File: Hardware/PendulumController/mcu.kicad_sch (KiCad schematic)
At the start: 21 parts, among them J201 Tag Connect, SW201 RESET, SW202 START_SW, SW203 STOP/MODE_SW, U201 ATmega328P-A, Y201 16mHz

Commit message: Cleanup board layout, cleanup firmware and go to bed, this is a sturdy place to start a new project!
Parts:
- J201: value Tag Connect -> ICSP
- U201: value ATmega328P-A -> ATmega328P
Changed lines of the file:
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@@
     (in_bom yes) (on_board yes)
     (property "Reference" "J201" (id 0) (at 41.91 147.32 0))
-    (property "Value" "Tag Connect" (id 1) (at 41.275 162.56 0))
+    (property "Value" "ICSP" (id 1) (at 41.91 162.56 0))
     (property "Footprint" "Connector:Tag-Connect_TC2050-IDC-FP_2x05_P1.27mm_Vertical" (id 2) (at 40.64 154.94 0)
       (effects (font (size 1.27 1.27)) hide)
@@
       (effects (font (size 1.27 1.27)) (justify left))
     )
-    (property "Value" "ATmega328P-A" (id 1) (at 43.815 116.84 0)
+    (property "Value" "ATmega328P" (id 1) (at 43.815 116.84 0)
       (effects (font (size 1.27 1.27)) (justify left))
     )

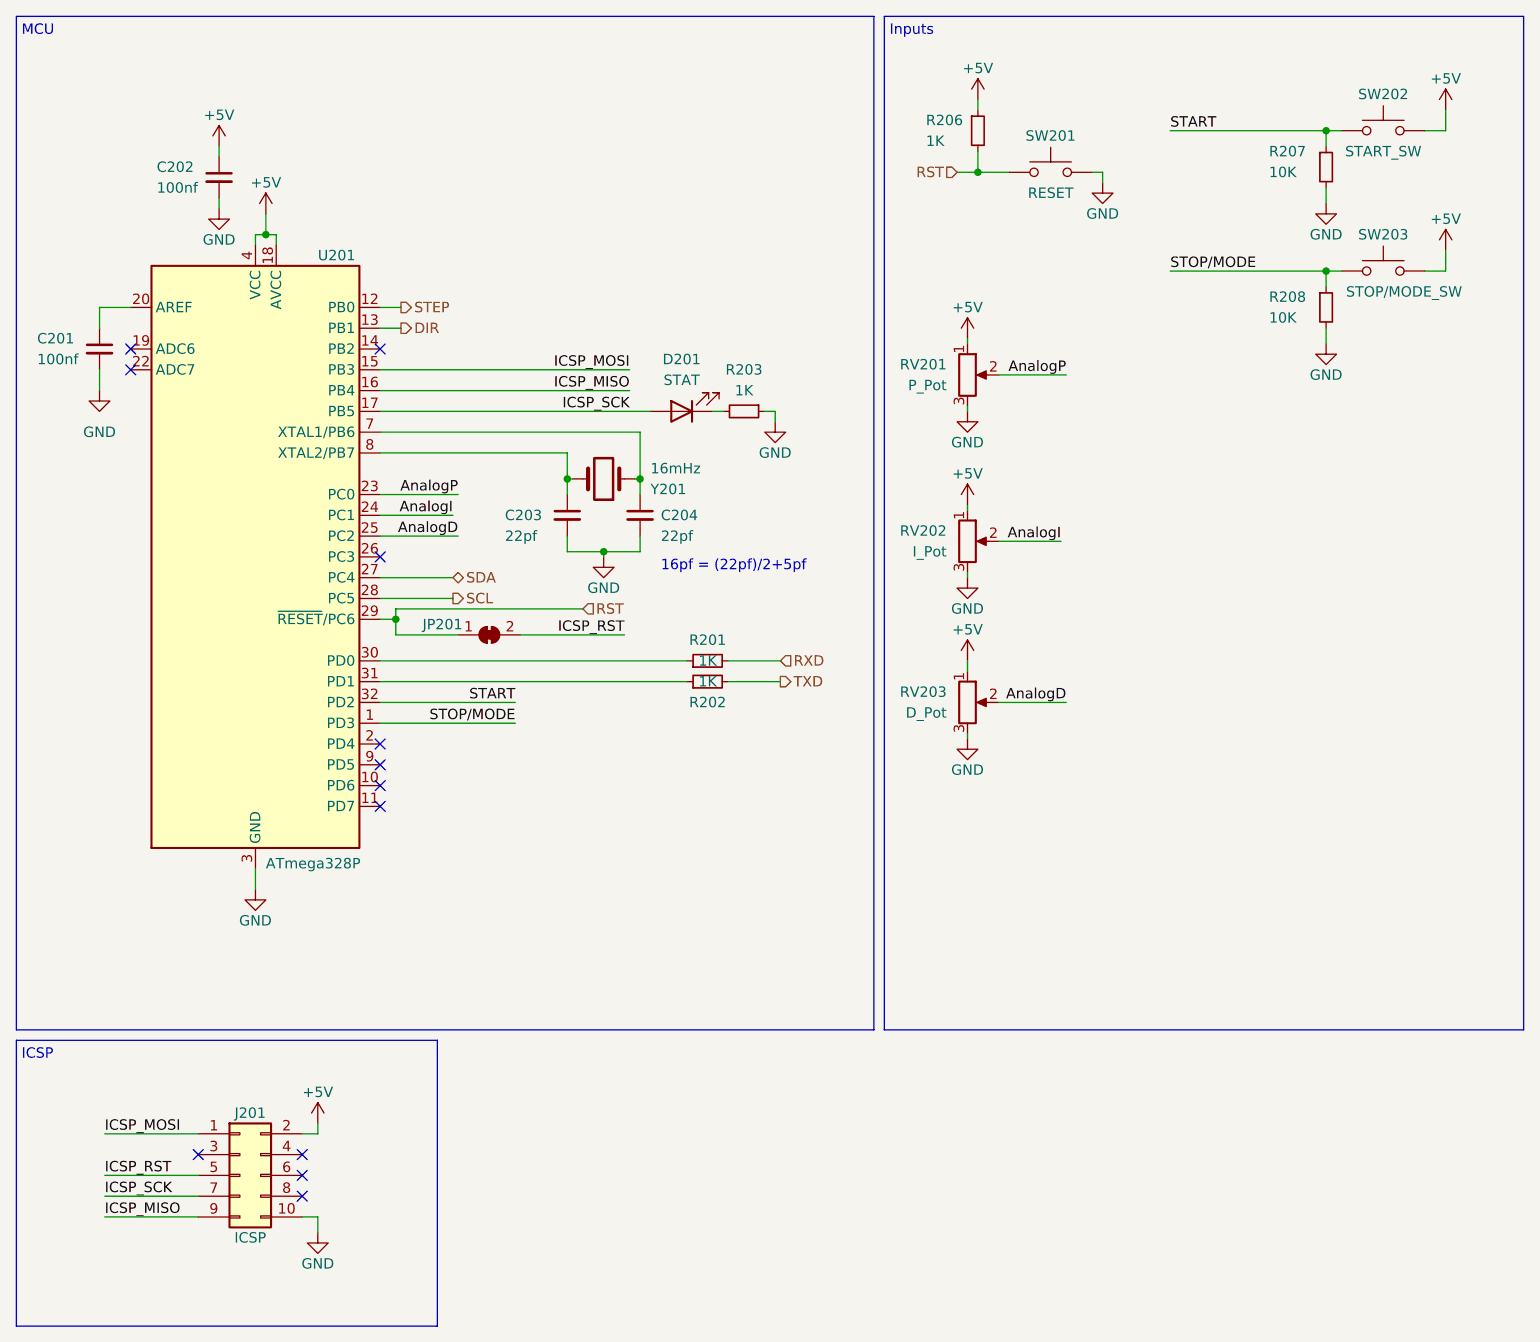
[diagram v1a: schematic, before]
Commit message: Add TFT connector
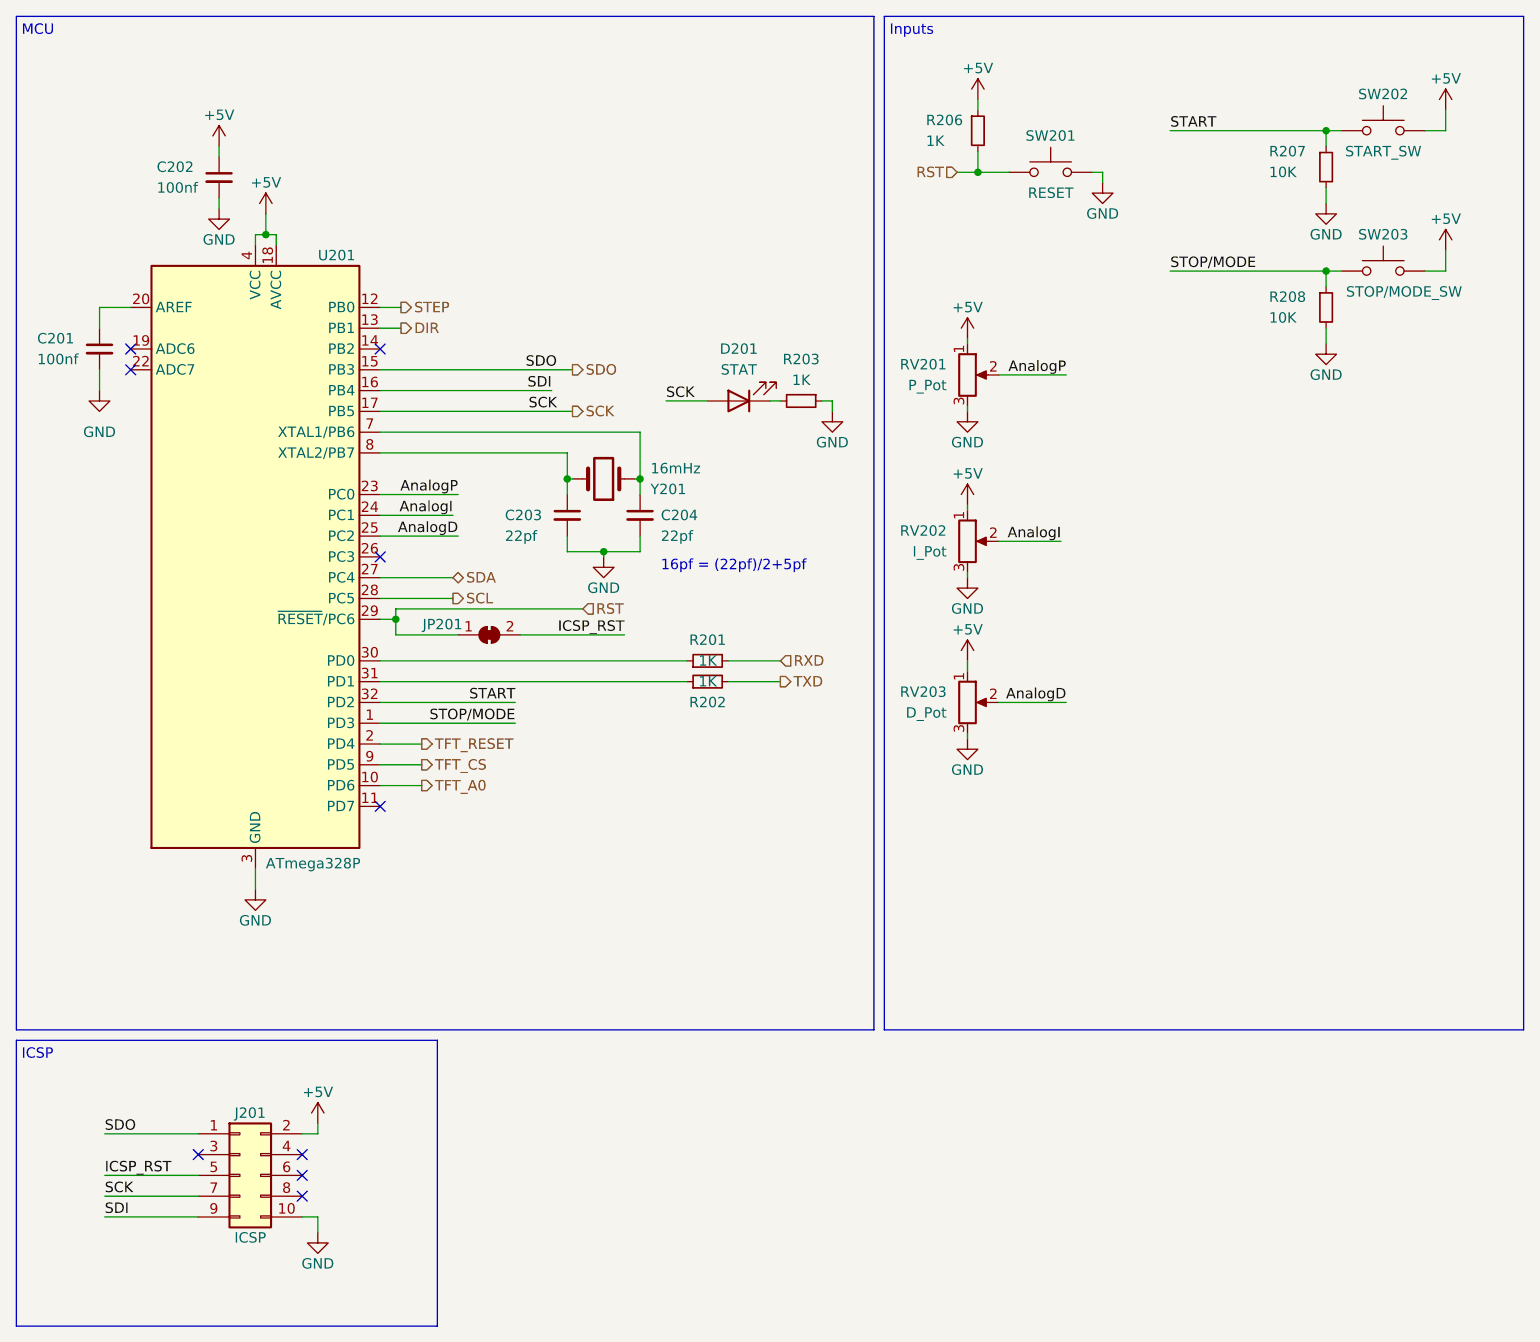
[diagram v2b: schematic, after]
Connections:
- net TFT_A0: now reaches U201.10 (PD6)
- net TFT_RESET: now reaches U201.2 (PD4)
- net TFT_CS: now reaches U201.9 (PD5)
- net ICSP_MISO renamed SDI
- net ICSP_MOSI renamed SDO
- net ICSP_SCK renamed SCK
- no-connect marks 12 -> 9

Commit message: V1 Board (#3)
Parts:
- added J202: Limit, Connector_JST:JST_EH_B2B-EH-A_1x02_P2.50mm_Vertical, symbol Connector:Conn_01x02_Male
- RV201, RV202, RV203: footprint (none) -> Connector_JST:JST_EH_B3B-EH-A_1x03_P2.50mm_Vertical
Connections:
- net SCL is gone; now on net AnalogD: U201.28 (PC5)
- net SDA is gone; now on net AnalogI: U201.27 (PC4)
- net +5V: now also J202.1 (Pin_1)
- net AnalogD: no longer U201.25 (PC2)
- net AnalogI: no longer U201.24 (PC1)
- net AnalogP: now also U201.26 (PC3); no longer U201.23 (PC0)
- net DIR: now also U201.24 (PC1); no longer U201.13 (PB1)
- net SCK: no longer D201.2 (A)
- net START: now also U201.13 (PB1), J202.2 (Pin_2); no longer U201.32 (PD2)
- net STEP: now also U201.23 (PC0); no longer U201.12 (PB0)
- net STOP/MODE: now also U201.12 (PB0); no longer U201.1 (PD3)
- net TFT_DC: now reaches U201.11 (PD7)
- net STAT_LED: now reaches U201.14 (PB2)
- net STAT_LED: now also D201.2 (A)
- net TFT_A0 renamed SD_CS
- new net EN: U201.25 (PC2)
- new net EncA: U201.32 (PD2)
- new net EncB: U201.1 (PD3)
- no-connect marks 9 -> 6
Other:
- note added: "Start Switch doubles as limit"

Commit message: Firmware (#15)
Merged for PRR
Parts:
- C201, C202: value 100nf -> 100nF
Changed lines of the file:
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@@
       (effects (font (size 1.27 1.27)) (justify left))
     )
-    (property "Value" "100nf" (id 1) (at 30.48 34.29 0)
+    (property "Value" "100nF" (id 1) (at 30.48 34.29 0)
       (effects (font (size 1.27 1.27)) (justify left))
     )
@@
       (effects (font (size 1.27 1.27)) (justify left))
     )
-    (property "Value" "100nf" (id 1) (at 15.875 55.245 0)
+    (property "Value" "100nF" (id 1) (at 15.875 55.245 0)
       (effects (font (size 1.27 1.27)) (justify left))
     )
